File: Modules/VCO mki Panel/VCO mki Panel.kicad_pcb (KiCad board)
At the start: 2 copper layers, 0 parts

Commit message: VCO mki in progress
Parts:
- added H1: MountingHole_Rails, SynthStuff:MountingHole_3.2mm_M3_Pad4mm, F.Cu at (54.0, 54.0)
- added H10: FM Lin, SynthStuff:Pot_Cutout_Tiny, F.Cu at (87.5, 172.5)
- added H11: PWM Mod, SynthStuff:Pot_Cutout_Tiny, F.Cu at (112.5, 172.5)
- added H12: Shape Mod, SynthStuff:Pot_Cutout_Tiny, F.Cu at (137.5, 172.5)
- added H13: Sin, SynthStuff:Jack_6.35mm_Cutout_Output_v5, F.Cu at (62.5, 228.8)
- added H14: Tri, SynthStuff:Jack_6.35mm_Cutout_Output_v5, F.Cu at (87.5, 228.8)
- added H15: Sqr, SynthStuff:Jack_6.35mm_Cutout_Output_v5, F.Cu at (112.5, 228.8)
- added H16: Saw/Var, SynthStuff:Jack_6.35mm_Cutout_Output_v5, F.Cu at (137.5, 228.8)
- added H17: CV, SynthStuff:Jack_6.35mm_Cutout_v2, F.Cu at (62.5, 206.2)
- added H18: Lin FM, SynthStuff:Jack_6.35mm_Cutout_v2, F.Cu at (87.5, 206.2)
- added H19: PWM Mod, SynthStuff:Jack_6.35mm_Cutout_v2, F.Cu at (112.5, 206.2)
- added H2: MountingHole_Rails, SynthStuff:MountingHole_3.2mm_M3_Pad4mm, F.Cu at (146.0, 54.0)
- added H20: Shape Mod, SynthStuff:Jack_6.35mm_Cutout_v2, F.Cu at (137.5, 206.2)
- added H21: Calib 1, MountingHole:MountingHole_3.2mm_M3, F.Cu at (92.0, 155.0)
- added H22: Calib 2, MountingHole:MountingHole_3.2mm_M3, F.Cu at (100.0, 155.0)
- added H23: Calib 3, MountingHole:MountingHole_3.2mm_M3, F.Cu at (108.0, 155.0)
- added H24: Sync, SynthStuff:Jack_6.35mm_Cutout_v2, F.Cu at (62.5, 172.5)
- added H3: MountingHole_Rails, SynthStuff:MountingHole_3.2mm_M3_Pad4mm, F.Cu at (54.0, 246.0)
- added H4: MountingHole_Rails, SynthStuff:MountingHole_3.2mm_M3_Pad4mm, F.Cu at (146.0, 246.0)
- added H5: Coarse, SynthStuff:Pot_Cutout_Large, F.Cu at (75.0, 82.5)
- added H6: Shape, SynthStuff:Pot_Cutout_Large, F.Cu at (125.0, 82.5)
- added H7: Fine, SynthStuff:Pot_Cutout_Medium, F.Cu at (70.0, 127.5)
- added H8: PWM, SynthStuff:Pot_Cutout_Medium, F.Cu at (130.0, 127.5)
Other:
- board outline added: 100 x 200 mm

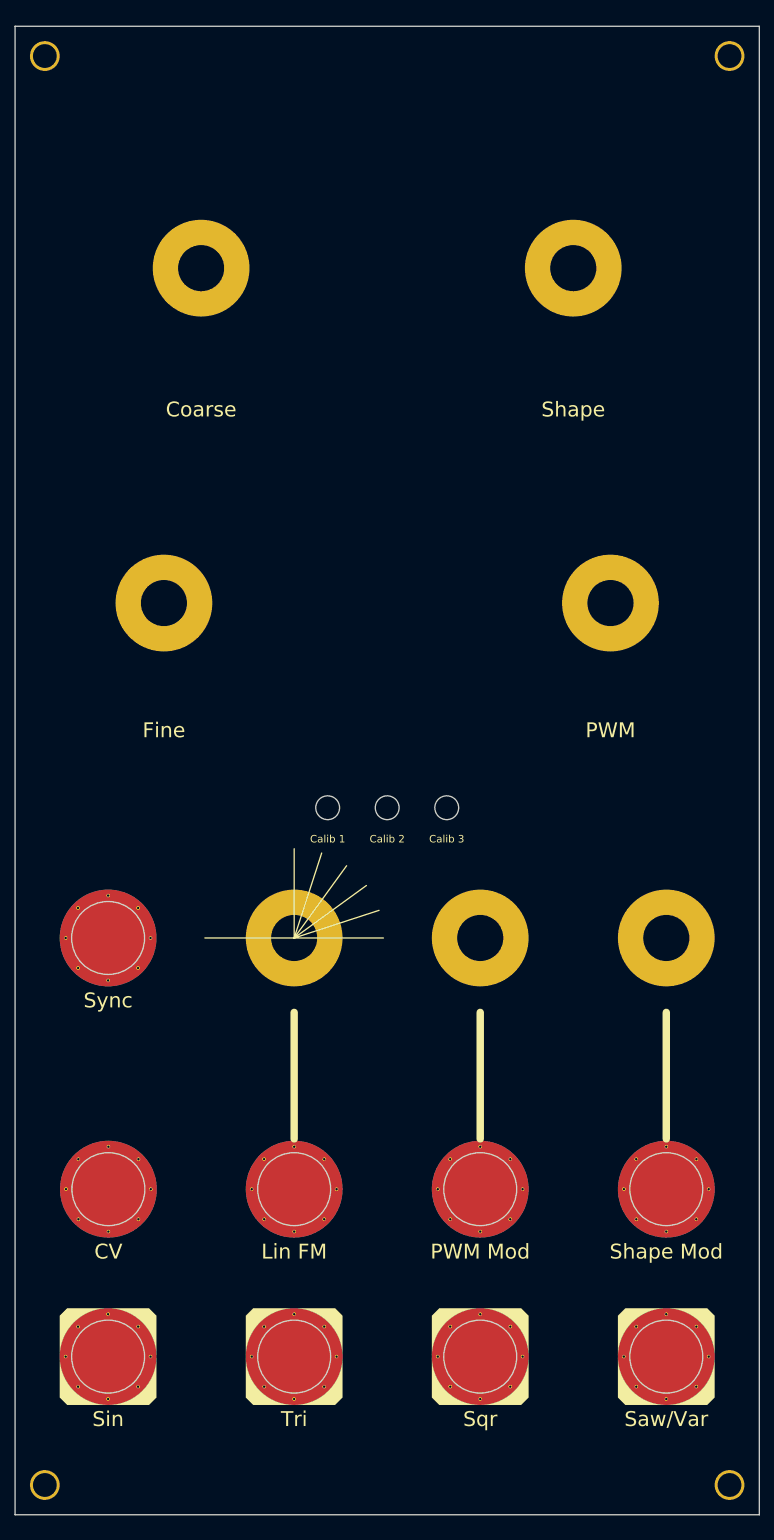
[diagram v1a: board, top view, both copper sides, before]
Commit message: Reconfigured controls in VCO mki
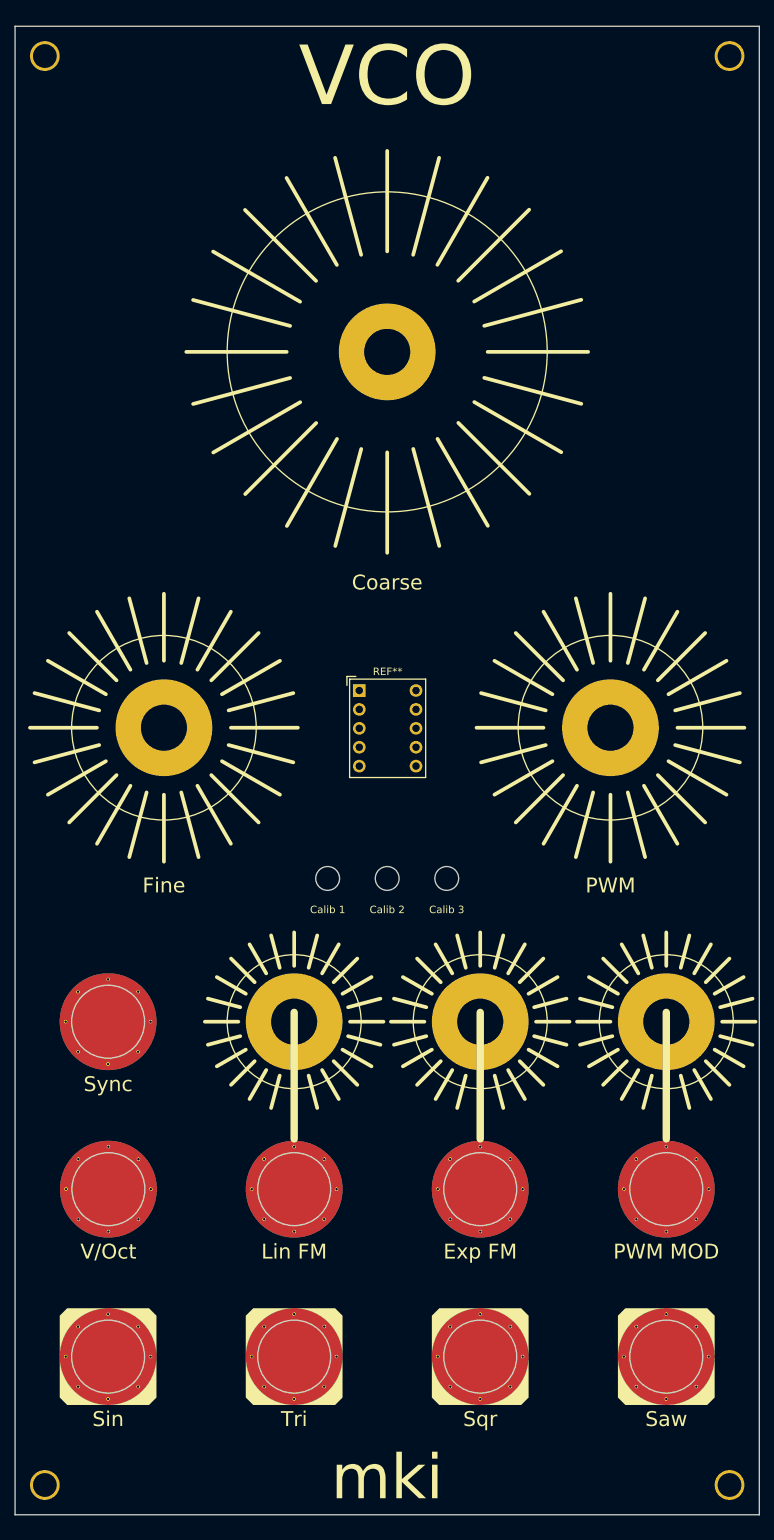
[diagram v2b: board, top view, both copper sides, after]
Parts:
- removed H6: Shape, SynthStuff:Pot_Cutout_Large
- added REF**: Sx39-1xxxxx, Display_7Segment:Sx39-1xxxxx, F.Cu at (96.2, 139.2)
- H16: value Saw/Var -> Saw
- H17: value CV -> V/Oct
- H19: value PWM Mod -> Exp FM
- H20: value Shape Mod -> PWM MOD
- H5: footprint SynthStuff:Pot_Cutout_Large -> SynthStuff:Pot_Cutout_Huge
- moved H5 27.4 mm to (100.0, 93.8)
- moved H7 16.8 mm to (70.0, 144.2)
- moved H8 16.8 mm to (130.0, 144.2)
- moved H10 11.2 mm to (87.5, 183.8)
- moved H11 11.2 mm to (112.5, 183.8)
- moved H12 11.2 mm to (137.5, 183.8)
- moved H24 11.2 mm to (62.5, 183.8)
- moved H21 9.50 mm to (92.0, 164.5)
- moved H22 9.50 mm to (100.0, 164.5)
- moved H23 9.50 mm to (108.0, 164.5)
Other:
- board text added: "VCO"
- board text added: "mki"

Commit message: Positioned Seg Disp and LEDs holes
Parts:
- removed the REF** at (96.2, 139.2)
- added REF**: MountingHole_3mm, MountingHole:MountingHole_3mm, F.Cu at (93.0, 158.0)
- added REF**: MountingHole_3mm, MountingHole:MountingHole_3mm, F.Cu at (107.0, 131.0)
- added REF**: MountingHole_3mm, MountingHole:MountingHole_3mm, F.Cu at (107.0, 158.0)
- added REF**: MountingHole_3mm, MountingHole:MountingHole_3mm, F.Cu at (100.0, 158.0)
- added REF**: MountingHole_3mm, MountingHole:MountingHole_3mm, F.Cu at (93.0, 131.0)
- added REF**: 7SegmentLED_LTS6760_LTS6780, Display_7Segment:7SegmentLED_LTS6760_LTS6780, F.Cu at (94.9, 152.0)
- moved H21 1.50 mm to (92.0, 166.0)
- moved H22 1.50 mm to (100.0, 166.0)
- moved H23 1.50 mm to (108.0, 166.0)

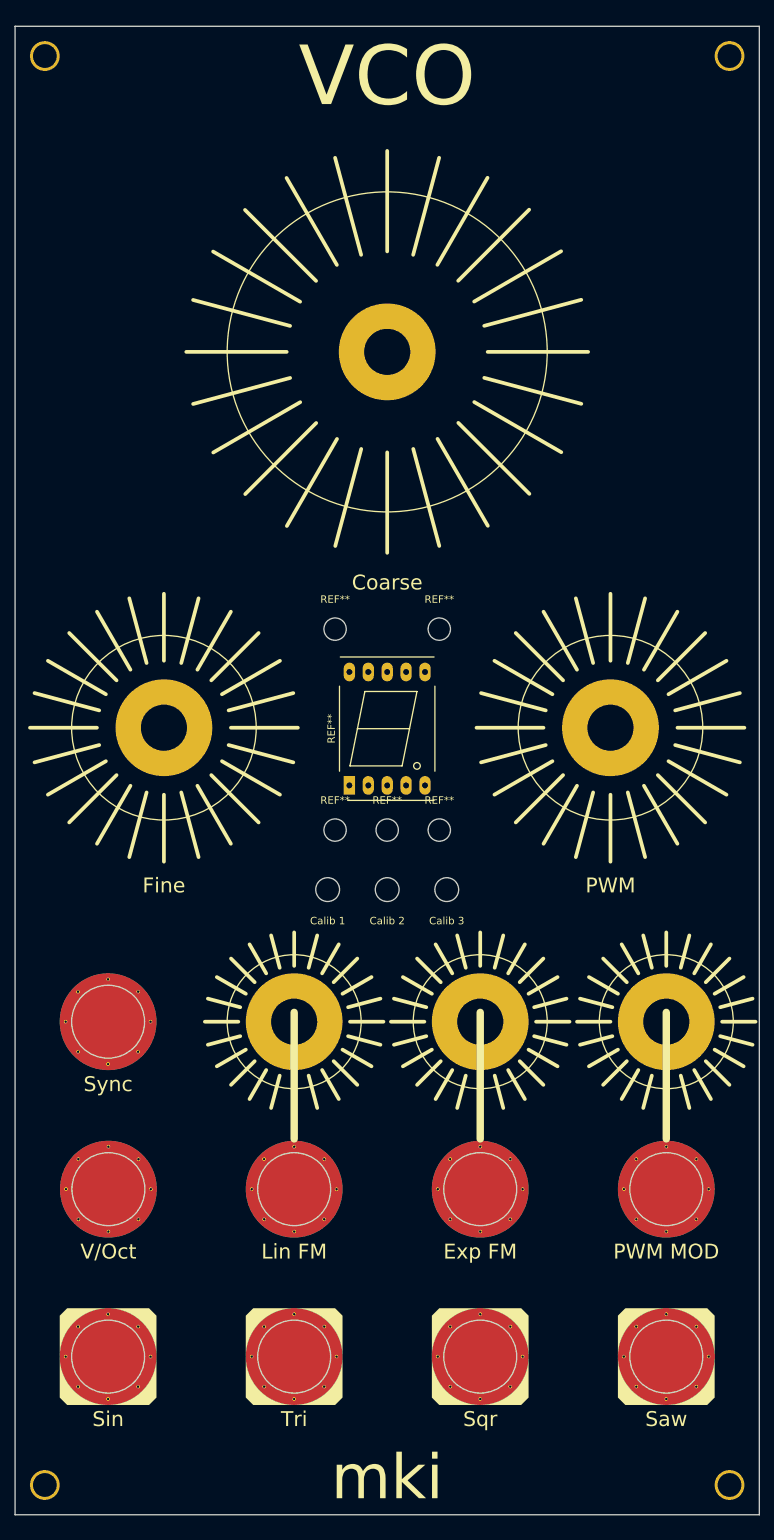
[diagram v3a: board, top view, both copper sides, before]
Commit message: Finished VCO mki panel layout
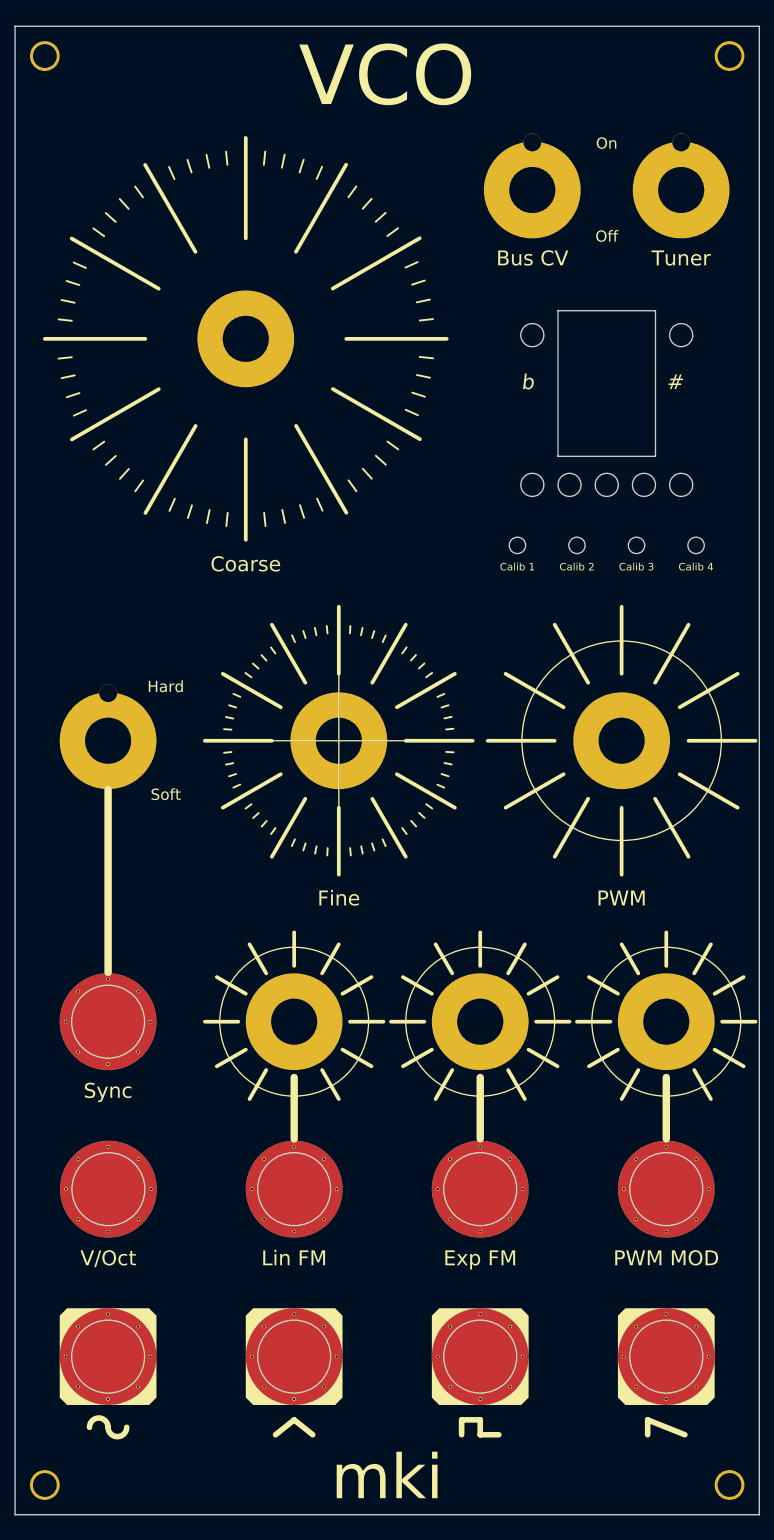
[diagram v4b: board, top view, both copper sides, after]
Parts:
- added H24: Calib 4, MountingHole:MountingHole_2.2mm_M2_DIN965, F.Cu at (141.5, 119.8)
- added REF**: Bus CV, SynthStuff:Toggle_Switch_Cutout, F.Cu at (119.5, 72.0)
- added REF**: MountingHole_LED_3mm, SynthStuff:MountingHole_LED_3mm, F.Cu at (139.5, 111.6)
- added REF**: Tuner, SynthStuff:Toggle_Switch_Cutout, F.Cu at (139.5, 72.0)
- added REF**: Hard Sync, SynthStuff:Toggle_Switch_Cutout, F.Cu at (62.5, 146.0)
- added REF**: MountingHole_LED_3mm, SynthStuff:MountingHole_LED_3mm, F.Cu at (119.5, 111.6)
- H21, H22, H23: footprint MountingHole:MountingHole_3.2mm_M3 -> MountingHole:MountingHole_2.2mm_M2_DIN965
- H5: footprint SynthStuff:Pot_Cutout_Huge -> SynthStuff:Pot_Cutout_Huge_v2
- H7: footprint SynthStuff:Pot_Cutout_Medium -> SynthStuff:Pot_Cutout_Medium_v2
- REF** (x5): value MountingHole_3mm -> MountingHole_LED_3mm; footprint MountingHole:MountingHole_3mm -> SynthStuff:MountingHole_LED_3mm
- REF**: value 7SegmentLED_LTS6760_LTS6780 -> 7Segment_Cutout; footprint Display_7Segment:7SegmentLED_LTS6760_LTS6780 -> SynthStuff:7Segment_Cutout
- moved REF** 56.1 mm to (124.5, 111.6)
- moved REF** 55.0 mm to (124.4, 105.6)
- moved REF** 55.0 mm to (129.5, 111.6)
- moved REF** 53.9 mm to (134.5, 111.6)
- moved H21 52.8 mm to (117.5, 119.8)
- moved H22 52.8 mm to (125.5, 119.8)
- moved H23 52.8 mm to (133.5, 119.8)
- moved REF** 51.2 mm to (139.5, 91.5)
- moved REF** 47.6 mm to (119.5, 91.5)
- moved H7 23.6 mm to (93.5, 146.0)
- moved H5 19.1 mm to (81.0, 92.0)
- moved H8 2.30 mm to (131.5, 146.0)
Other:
- board text added: "#"
- board text added: "Hard"
- board text added: "Off"
- board text added: "On"
- board text added: "Soft"
- board text added: "b"
